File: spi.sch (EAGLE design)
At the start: 5 parts, among them IC2 25AA080SN, IC3 25AA080P, X1 2510-

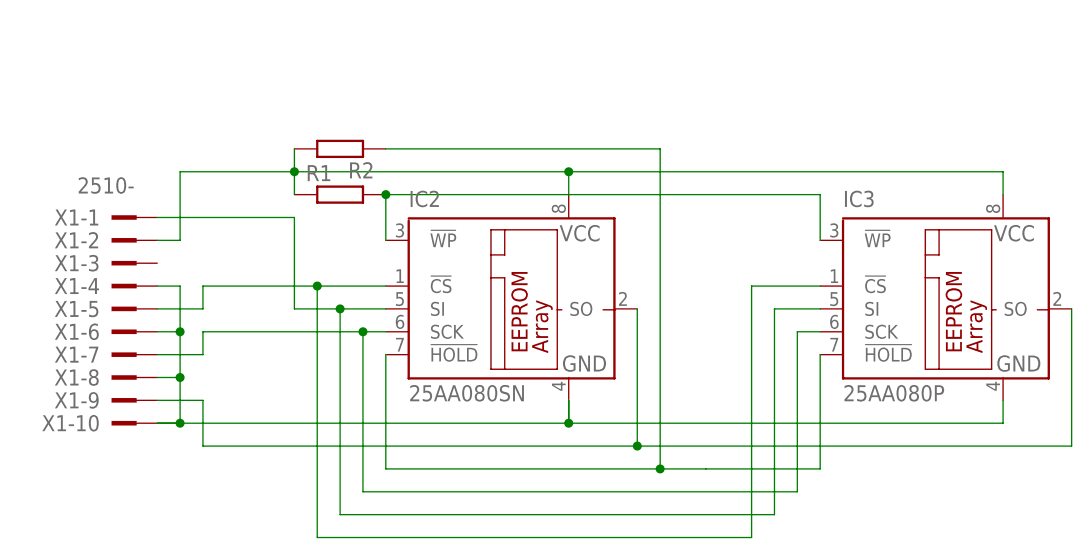
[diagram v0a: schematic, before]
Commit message: Added ground polygon
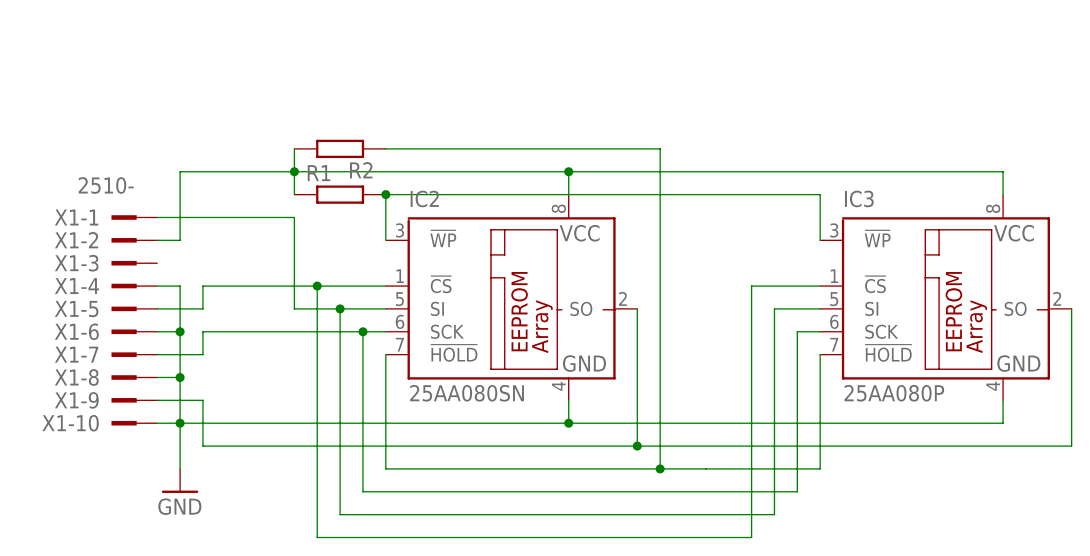
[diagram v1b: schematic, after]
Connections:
- net N$1 renamed GND
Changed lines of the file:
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@@
 <part name="R1" library="eagle-ltspice" library_urn="urn:adsk.eagle:library:217" deviceset="R" device="0207/10" package3d_urn="urn:adsk.eagle:package:13275/1"/>
 <part name="R2" library="eagle-ltspice" library_urn="urn:adsk.eagle:library:217" deviceset="R" device="0207/10" package3d_urn="urn:adsk.eagle:package:13275/1"/>
+<part name="GND1" library="supply1" library_urn="urn:adsk.eagle:library:371" deviceset="GND" device=""/>
 </parts>
 <sheets>
@@
 <instance part="R1" gate="G$1" x="10.16" y="78.74"/>
 <instance part="R2" gate="G$1" x="10.16" y="83.82" rot="R180"/>
+<instance part="GND1" gate="1" x="-7.62" y="45.72"/>
 </instances>
 <busses>
 </busses>
 <nets>
-<net name="N$1" class="0">
-<segment>
-<pinref part="IC2" gate="G$1" pin="GND"/>
-<wire x1="35.56" y1="55.88" x2="35.56" y2="53.34" width="0.1524" layer="91"/>
-<wire x1="35.56" y1="53.34" x2="83.82" y2="53.34" width="0.1524" layer="91"/>
-<pinref part="IC3" gate="G$1" pin="GND"/>
-<wire x1="83.82" y1="53.34" x2="83.82" y2="55.88" width="0.1524" layer="91"/>
-<wire x1="35.56" y1="55.88" x2="35.56" y2="53.34" width="0.1524" layer="91"/>
-<junction x="35.56" y="53.34"/>
-<wire x1="35.56" y1="53.34" x2="-7.62" y2="53.34" width="0.1524" layer="91"/>
-<pinref part="X1" gate="-4" pin="KL"/>
-<wire x1="-7.62" y1="53.34" x2="-10.16" y2="53.34" width="0.1524" layer="91"/>
-<wire x1="-10.16" y1="68.58" x2="-7.62" y2="68.58" width="0.1524" layer="91"/>
-<wire x1="-7.62" y1="68.58" x2="-7.62" y2="63.5" width="0.1524" layer="91"/>
-<pinref part="X1" gate="-6" pin="KL"/>
-<wire x1="-7.62" y1="63.5" x2="-10.16" y2="63.5" width="0.1524" layer="91"/>
-<pinref part="X1" gate="-8" pin="KL"/>
-<wire x1="-10.16" y1="58.42" x2="-7.62" y2="58.42" width="0.1524" layer="91"/>
-<wire x1="-7.62" y1="58.42" x2="-7.62" y2="63.5" width="0.1524" layer="91"/>
-<junction x="-7.62" y="63.5"/>
-<pinref part="X1" gate="-10" pin="KL"/>
-<wire x1="-10.16" y1="53.34" x2="-7.62" y2="53.34" width="0.1524" layer="91"/>
-<wire x1="-7.62" y1="53.34" x2="-7.62" y2="58.42" width="0.1524" layer="91"/>
-<junction x="-7.62" y="58.42"/>
-<junction x="-7.62" y="53.34"/>
-</segment>
-</net>
 <net name="N$2" class="0">
 <segment>
@@
 </segment>
 </net>
+<net name="GND" class="0">
+<segment>
+<pinref part="IC2" gate="G$1" pin="GND"/>
+<wire x1="35.56" y1="53.34" x2="83.82" y2="53.34" width="0.1524" layer="91"/>
+<pinref part="IC3" gate="G$1" pin="GND"/>
+<wire x1="83.82" y1="53.34" x2="83.82" y2="55.88" width="0.1524" layer="91"/>
+<wire x1="35.56" y1="55.88" x2="35.56" y2="53.34" width="0.1524" layer="91"/>
+<junction x="35.56" y="53.34"/>
+<wire x1="35.56" y1="53.34" x2="-7.62" y2="53.34" width="0.1524" layer="91"/>
+<pinref part="X1" gate="-4" pin="KL"/>
+<wire x1="-10.16" y1="68.58" x2="-7.62" y2="68.58" width="0.1524" layer="91"/>
+<wire x1="-7.62" y1="68.58" x2="-7.62" y2="63.5" width="0.1524" layer="91"/>
+<pinref part="X1" gate="-6" pin="KL"/>
+<wire x1="-7.62" y1="63.5" x2="-10.16" y2="63.5" width="0.1524" layer="91"/>
+<pinref part="X1" gate="-8" pin="KL"/>
+<wire x1="-10.16" y1="58.42" x2="-7.62" y2="58.42" width="0.1524" layer="91"/>
+<wire x1="-7.62" y1="58.42" x2="-7.62" y2="63.5" width="0.1524" layer="91"/>
+<junction x="-7.62" y="63.5"/>
+<pinref part="X1" gate="-10" pin="KL"/>
+<wire x1="-10.16" y1="53.34" x2="-7.62" y2="53.34" width="0.1524" layer="91"/>
+<wire x1="-7.62" y1="53.34" x2="-7.62" y2="58.42" width="0.1524" layer="91"/>
+<junction x="-7.62" y="58.42"/>
+<junction x="-7.62" y="53.34"/>
+<pinref part="GND1" gate="1" pin="GND"/>
+<wire x1="-7.62" y1="53.34" x2="-7.62" y2="48.26" width="0.1524" layer="91"/>
+</segment>
+</net>

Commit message: Renamed net
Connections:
- net N$2 renamed VCC
- net N$3 renamed SO
- net N$4 renamed HOLD
- net N$5 renamed SCK
- net N$6 renamed SI
- net N$7 renamed CS
- net N$8 renamed WP
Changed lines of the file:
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@@
 <instance part="X1" gate="-3" x="-15.24" y="71.12"/>
 <instance part="X1" gate="-4" x="-15.24" y="68.58"/>
-<instance part="X1" gate="-5" x="-15.24" y="66.04"/>
+<instance part="X1" gate="-5" x="-15.24" y="66.04" smashed="yes">
+<attribute name="NAME" x="-16.51" y="66.929" size="1.778" layer="95" rot="R180"/>
+</instance>
 <instance part="X1" gate="-6" x="-15.24" y="63.5"/>
 <instance part="X1" gate="-7" x="-15.24" y="60.96"/>
@@
 </busses>
 <nets>
-<net name="N$2" class="0">
+<net name="VCC" class="0">
 <segment>
 <pinref part="IC2" gate="G$1" pin="VCC"/>
@@
 </segment>
 </net>
-<net name="N$3" class="0">
+<net name="SO" class="0">
 <segment>
 <pinref part="IC2" gate="G$1" pin="SO"/>
@@
 </segment>
 </net>
-<net name="N$4" class="0">
+<net name="HOLD" class="0">
 <segment>
 <pinref part="IC2" gate="G$1" pin="!HOLD"/>
@@
 </segment>
 </net>
-<net name="N$5" class="0">
+<net name="SCK" class="0">
 <segment>
 <pinref part="IC2" gate="G$1" pin="SCK"/>
@@
 </segment>
 </net>
-<net name="N$6" class="0">
+<net name="SI" class="0">
 <segment>
 <pinref part="IC2" gate="G$1" pin="SI"/>
@@
 </segment>
 </net>
-<net name="N$7" class="0">
+<net name="CS" class="0">
 <segment>
 <pinref part="IC2" gate="G$1" pin="!CS"/>
@@
 </segment>
 </net>
-<net name="N$8" class="0">
+<net name="WP" class="0">
 <segment>
 <pinref part="IC2" gate="G$1" pin="!WP"/>

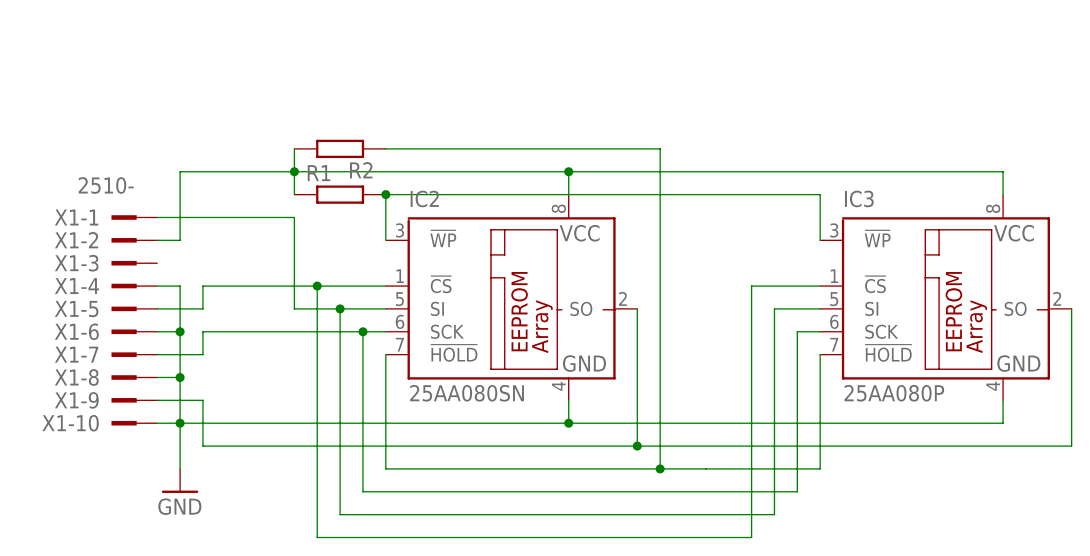
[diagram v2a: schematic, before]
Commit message: Fixed spi25 label
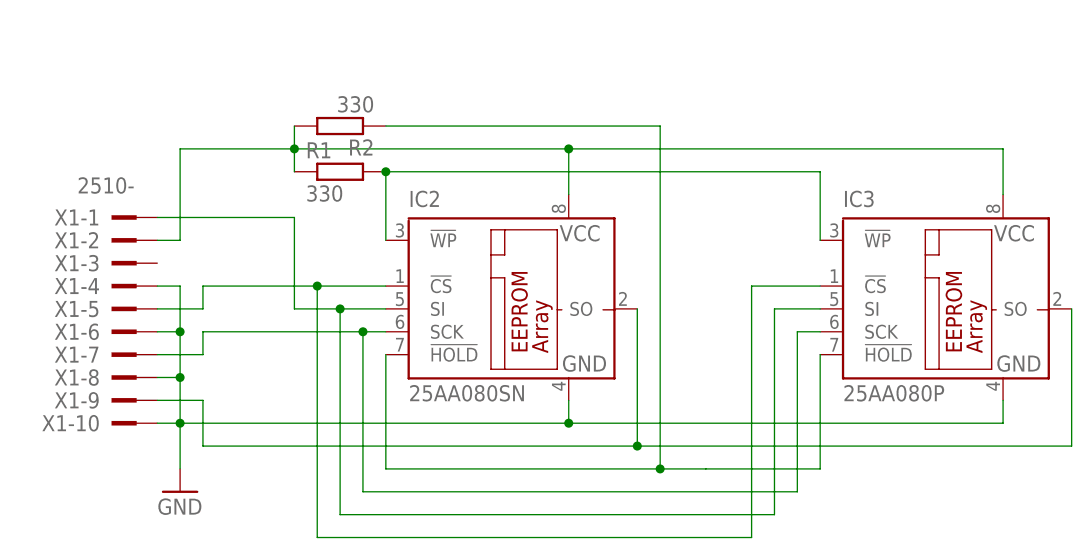
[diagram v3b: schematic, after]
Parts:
- R1, R2: value (none) -> 330
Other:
- moved on the sheet: R1, R2
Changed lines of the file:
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@@
 <part name="IC3" library="microchip" library_urn="urn:adsk.eagle:library:294" deviceset="25*" device="P" package3d_urn="urn:adsk.eagle:package:20796/2" technology="AA080"/>
 <part name="X1" library="con-3m" library_urn="urn:adsk.eagle:library:119" deviceset="2510-" device="" package3d_urn="urn:adsk.eagle:package:5571/1"/>
-<part name="R1" library="eagle-ltspice" library_urn="urn:adsk.eagle:library:217" deviceset="R" device="0207/10" package3d_urn="urn:adsk.eagle:package:13275/1"/>
-<part name="R2" library="eagle-ltspice" library_urn="urn:adsk.eagle:library:217" deviceset="R" device="0207/10" package3d_urn="urn:adsk.eagle:package:13275/1"/>
+<part name="R1" library="eagle-ltspice" library_urn="urn:adsk.eagle:library:217" deviceset="R" device="0207/10" package3d_urn="urn:adsk.eagle:package:13275/1" value="330"/>
+<part name="R2" library="eagle-ltspice" library_urn="urn:adsk.eagle:library:217" deviceset="R" device="0207/10" package3d_urn="urn:adsk.eagle:package:13275/1" value="330"/>
 <part name="GND1" library="supply1" library_urn="urn:adsk.eagle:library:371" deviceset="GND" device=""/>
 </parts>
@@
 <instance part="X1" gate="-9" x="-15.24" y="55.88"/>
 <instance part="X1" gate="-10" x="-15.24" y="53.34"/>
-<instance part="R1" gate="G$1" x="10.16" y="78.74"/>
-<instance part="R2" gate="G$1" x="10.16" y="83.82" rot="R180"/>
+<instance part="R1" gate="G$1" x="10.16" y="81.28"/>
+<instance part="R2" gate="G$1" x="10.16" y="86.36" rot="R180"/>
 <instance part="GND1" gate="1" x="-7.62" y="45.72"/>
 </instances>
@@
 <segment>
 <pinref part="IC2" gate="G$1" pin="VCC"/>
-<wire x1="35.56" y1="78.74" x2="35.56" y2="81.28" width="0.1524" layer="91"/>
-<wire x1="35.56" y1="81.28" x2="83.82" y2="81.28" width="0.1524" layer="91"/>
+<wire x1="35.56" y1="78.74" x2="35.56" y2="83.82" width="0.1524" layer="91"/>
+<wire x1="35.56" y1="83.82" x2="83.82" y2="83.82" width="0.1524" layer="91"/>
 <pinref part="IC3" gate="G$1" pin="VCC"/>
-<wire x1="83.82" y1="81.28" x2="83.82" y2="78.74" width="0.1524" layer="91"/>
+<wire x1="83.82" y1="83.82" x2="83.82" y2="78.74" width="0.1524" layer="91"/>
 <pinref part="X1" gate="-2" pin="KL"/>
 <wire x1="-10.16" y1="73.66" x2="-7.62" y2="73.66" width="0.1524" layer="91"/>
-<wire x1="-7.62" y1="73.66" x2="-7.62" y2="81.28" width="0.1524" layer="91"/>
-<wire x1="-7.62" y1="81.28" x2="5.08" y2="81.28" width="0.1524" layer="91"/>
-<junction x="35.56" y="81.28"/>
+<wire x1="-7.62" y1="73.66" x2="-7.62" y2="83.82" width="0.1524" layer="91"/>
+<wire x1="-7.62" y1="83.82" x2="5.08" y2="83.82" width="0.1524" layer="91"/>
+<junction x="35.56" y="83.82"/>
 <pinref part="R1" gate="G$1" pin="1"/>
-<wire x1="5.08" y1="81.28" x2="35.56" y2="81.28" width="0.1524" layer="91"/>
-<wire x1="5.08" y1="78.74" x2="5.08" y2="81.28" width="0.1524" layer="91"/>
-<junction x="5.08" y="81.28"/>
+<wire x1="5.08" y1="83.82" x2="35.56" y2="83.82" width="0.1524" layer="91"/>
+<wire x1="5.08" y1="81.28" x2="5.08" y2="83.82" width="0.1524" layer="91"/>
+<junction x="5.08" y="83.82"/>
 <pinref part="R2" gate="G$1" pin="2"/>
-<wire x1="5.08" y1="83.82" x2="5.08" y2="81.28" width="0.1524" layer="91"/>
+<wire x1="5.08" y1="86.36" x2="5.08" y2="83.82" width="0.1524" layer="91"/>
 </segment>
 </net>
@@
 <wire x1="63.5" y1="60.96" x2="63.5" y2="48.26" width="0.1524" layer="91"/>
 <pinref part="R2" gate="G$1" pin="1"/>
-<wire x1="15.24" y1="83.82" x2="45.72" y2="83.82" width="0.1524" layer="91"/>
-<wire x1="45.72" y1="83.82" x2="45.72" y2="48.26" width="0.1524" layer="91"/>
+<wire x1="15.24" y1="86.36" x2="45.72" y2="86.36" width="0.1524" layer="91"/>
+<wire x1="45.72" y1="86.36" x2="45.72" y2="48.26" width="0.1524" layer="91"/>
 <junction x="45.72" y="48.26"/>
 </segment>
@@
 <pinref part="IC2" gate="G$1" pin="!WP"/>
 <pinref part="R1" gate="G$1" pin="2"/>
-<wire x1="15.24" y1="73.66" x2="15.24" y2="78.74" width="0.1524" layer="91"/>
+<wire x1="15.24" y1="73.66" x2="15.24" y2="81.28" width="0.1524" layer="91"/>
 <pinref part="IC3" gate="G$1" pin="!WP"/>
-<wire x1="63.5" y1="73.66" x2="63.5" y2="78.74" width="0.1524" layer="91"/>
-<wire x1="63.5" y1="78.74" x2="15.24" y2="78.74" width="0.1524" layer="91"/>
-<junction x="15.24" y="78.74"/>
+<wire x1="63.5" y1="73.66" x2="63.5" y2="81.28" width="0.1524" layer="91"/>
+<wire x1="63.5" y1="81.28" x2="15.24" y2="81.28" width="0.1524" layer="91"/>
+<junction x="15.24" y="81.28"/>
 </segment>
 </net>

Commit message: Fixed polygon
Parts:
- R1, R2: value 330 -> (none); device eagle-ltspice:R0207/10 -> eagle-ltspice:R0204/7
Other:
- moved on the sheet: R1, R2
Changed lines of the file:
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@@
 <layer number="18" name="Vias" color="2" fill="1" visible="no" active="no"/>
 <layer number="19" name="Unrouted" color="6" fill="1" visible="no" active="no"/>
-<layer number="20" name="Dimension" color="15" fill="1" visible="no" active="no"/>
+<layer number="20" name="Dimension" color="24" fill="1" visible="no" active="no"/>
 <layer number="21" name="tPlace" color="7" fill="1" visible="no" active="no"/>
 <layer number="22" name="bPlace" color="7" fill="1" visible="no" active="no"/>
@@
 <layer number="48" name="Document" color="7" fill="1" visible="no" active="no"/>
 <layer number="49" name="Reference" color="7" fill="1" visible="no" active="no"/>
-<layer number="51" name="tDocu" color="6" fill="9" visible="no" active="no"/>
+<layer number="51" name="tDocu" color="7" fill="1" visible="no" active="no"/>
 <layer number="52" name="bDocu" color="7" fill="1" visible="no" active="no"/>
 <layer number="88" name="SimResults" color="9" fill="1" visible="yes" active="yes"/>
@@
 <part name="IC3" library="microchip" library_urn="urn:adsk.eagle:library:294" deviceset="25*" device="P" package3d_urn="urn:adsk.eagle:package:20796/2" technology="AA080"/>
 <part name="X1" library="con-3m" library_urn="urn:adsk.eagle:library:119" deviceset="2510-" device="" package3d_urn="urn:adsk.eagle:package:5571/1"/>
-<part name="R1" library="eagle-ltspice" library_urn="urn:adsk.eagle:library:217" deviceset="R" device="0207/10" package3d_urn="urn:adsk.eagle:package:13275/1" value="330"/>
-<part name="R2" library="eagle-ltspice" library_urn="urn:adsk.eagle:library:217" deviceset="R" device="0207/10" package3d_urn="urn:adsk.eagle:package:13275/1" value="330"/>
+<part name="R1" library="eagle-ltspice" library_urn="urn:adsk.eagle:library:217" deviceset="R" device="0204/7" package3d_urn="urn:adsk.eagle:package:13274/1"/>
+<part name="R2" library="eagle-ltspice" library_urn="urn:adsk.eagle:library:217" deviceset="R" device="0204/7" package3d_urn="urn:adsk.eagle:package:13274/1"/>
 <part name="GND1" library="supply1" library_urn="urn:adsk.eagle:library:371" deviceset="GND" device=""/>
 </parts>
@@
 <instance part="X1" gate="-9" x="-15.24" y="55.88"/>
 <instance part="X1" gate="-10" x="-15.24" y="53.34"/>
-<instance part="R1" gate="G$1" x="10.16" y="81.28"/>
-<instance part="R2" gate="G$1" x="10.16" y="86.36" rot="R180"/>
+<instance part="R1" gate="G$1" x="10.16" y="78.74" smashed="yes">
+<attribute name="NAME" x="6.35" y="80.2386" size="1.778" layer="95"/>
+<attribute name="VALUE" x="6.35" y="75.438" size="1.778" layer="96"/>
+</instance>
+<instance part="R2" gate="G$1" x="10.16" y="83.82" rot="R180"/>
 <instance part="GND1" gate="1" x="-7.62" y="45.72"/>
 </instances>
@@
 <segment>
 <pinref part="IC2" gate="G$1" pin="VCC"/>
-<wire x1="35.56" y1="78.74" x2="35.56" y2="83.82" width="0.1524" layer="91"/>
-<wire x1="35.56" y1="83.82" x2="83.82" y2="83.82" width="0.1524" layer="91"/>
+<wire x1="35.56" y1="78.74" x2="35.56" y2="81.28" width="0.1524" layer="91"/>
+<wire x1="35.56" y1="81.28" x2="83.82" y2="81.28" width="0.1524" layer="91"/>
 <pinref part="IC3" gate="G$1" pin="VCC"/>
-<wire x1="83.82" y1="83.82" x2="83.82" y2="78.74" width="0.1524" layer="91"/>
+<wire x1="83.82" y1="81.28" x2="83.82" y2="78.74" width="0.1524" layer="91"/>
 <pinref part="X1" gate="-2" pin="KL"/>
 <wire x1="-10.16" y1="73.66" x2="-7.62" y2="73.66" width="0.1524" layer="91"/>
-<wire x1="-7.62" y1="73.66" x2="-7.62" y2="83.82" width="0.1524" layer="91"/>
-<wire x1="-7.62" y1="83.82" x2="5.08" y2="83.82" width="0.1524" layer="91"/>
-<junction x="35.56" y="83.82"/>
+<wire x1="-7.62" y1="73.66" x2="-7.62" y2="81.28" width="0.1524" layer="91"/>
+<wire x1="-7.62" y1="81.28" x2="5.08" y2="81.28" width="0.1524" layer="91"/>
+<junction x="35.56" y="81.28"/>
 <pinref part="R1" gate="G$1" pin="1"/>
-<wire x1="5.08" y1="83.82" x2="35.56" y2="83.82" width="0.1524" layer="91"/>
-<wire x1="5.08" y1="81.28" x2="5.08" y2="83.82" width="0.1524" layer="91"/>
-<junction x="5.08" y="83.82"/>
+<wire x1="5.08" y1="81.28" x2="35.56" y2="81.28" width="0.1524" layer="91"/>
+<wire x1="5.08" y1="78.74" x2="5.08" y2="81.28" width="0.1524" layer="91"/>
+<junction x="5.08" y="81.28"/>
 <pinref part="R2" gate="G$1" pin="2"/>
-<wire x1="5.08" y1="86.36" x2="5.08" y2="83.82" width="0.1524" layer="91"/>
+<wire x1="5.08" y1="83.82" x2="5.08" y2="81.28" width="0.1524" layer="91"/>
 </segment>
 </net>
@@
 <wire x1="63.5" y1="60.96" x2="63.5" y2="48.26" width="0.1524" layer="91"/>
 <pinref part="R2" gate="G$1" pin="1"/>
-<wire x1="15.24" y1="86.36" x2="45.72" y2="86.36" width="0.1524" layer="91"/>
-<wire x1="45.72" y1="86.36" x2="45.72" y2="48.26" width="0.1524" layer="91"/>
+<wire x1="15.24" y1="83.82" x2="45.72" y2="83.82" width="0.1524" layer="91"/>
+<wire x1="45.72" y1="83.82" x2="45.72" y2="48.26" width="0.1524" layer="91"/>
 <junction x="45.72" y="48.26"/>
 </segment>
@@
 <pinref part="IC2" gate="G$1" pin="!WP"/>
 <pinref part="R1" gate="G$1" pin="2"/>
-<wire x1="15.24" y1="73.66" x2="15.24" y2="81.28" width="0.1524" layer="91"/>
+<wire x1="15.24" y1="73.66" x2="15.24" y2="78.74" width="0.1524" layer="91"/>
 <pinref part="IC3" gate="G$1" pin="!WP"/>
-<wire x1="63.5" y1="73.66" x2="63.5" y2="81.28" width="0.1524" layer="91"/>
-<wire x1="63.5" y1="81.28" x2="15.24" y2="81.28" width="0.1524" layer="91"/>
-<junction x="15.24" y="81.28"/>
-</segment>
-</net>
+<wire x1="63.5" y1="73.66" x2="63.5" y2="78.74" width="0.1524" layer="91"/>
+<wire x1="63.5" y1="78.74" x2="15.24" y2="78.74" width="0.1524" layer="91"/>
+<junction x="15.24" y="78.74"/>
+</segment>
+</net>

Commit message: Добавлены конденсаторы по питанию
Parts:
- added C1: 100n, resistor:C-EUC0805K
- added C2: 10 uF, resistor:CPOL-EUSMCD
- R1, R2: value (none) -> 330 Om
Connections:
- net GND: now also C1.2, C2.-
- net VCC: now also C1.1, C2.+
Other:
- moved on the sheet: R1, R2
